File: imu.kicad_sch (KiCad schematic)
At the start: 3 parts, among them U14 LSM6DSV16XTR

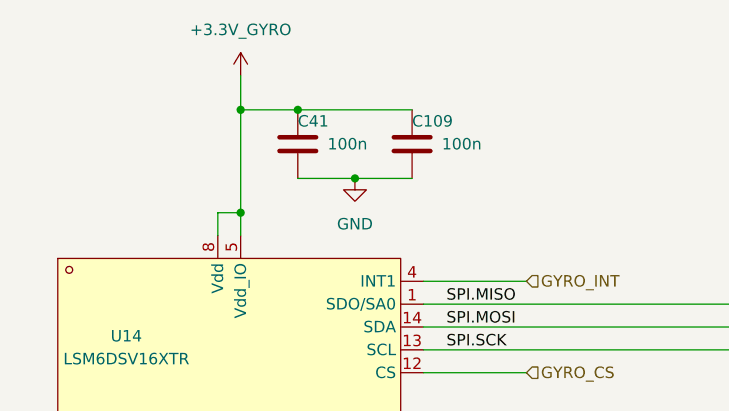
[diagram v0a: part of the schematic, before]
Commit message: fixed gyro power and rp2350 inductor
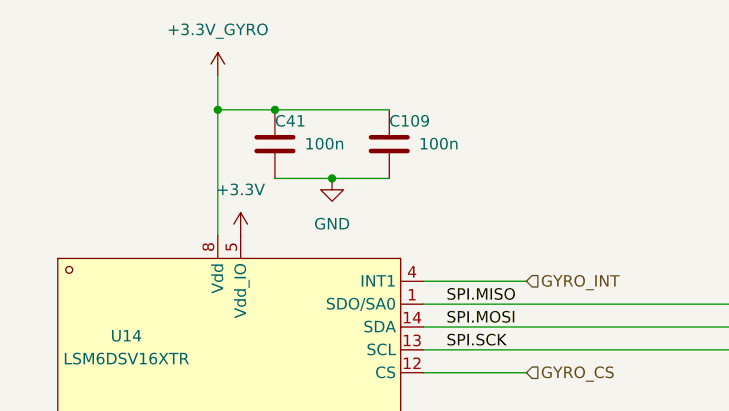
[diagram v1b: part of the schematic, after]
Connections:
- net +3.3V_GYRO: no longer U14.5 (Vdd_IO)
- new net +3.3V: U14.5 (Vdd_IO)
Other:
- moved on the sheet: C109, C41
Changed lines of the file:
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@@
 	(paper "A5")
 	(junction
-		(at 86.36 50.8)
+		(at 83.82 50.8)
 		(diameter 0)
 		(color 0 0 0 0)
@@
 	)
 	(junction
-		(at 73.66 43.18)
+		(at 71.12 43.18)
 		(diameter 0)
 		(color 0 0 0 0)
 	)
 	(junction
-		(at 80.01 43.18)
-		(diameter 0)
-		(color 0 0 0 0)
-	)
-	(junction
-		(at 73.66 54.61)
+		(at 77.47 43.18)
 		(diameter 0)
 		(color 0 0 0 0)
@@
 	(wire
 		(pts
-			(xy 73.66 43.18) (xy 80.01 43.18)
-		)
-		(stroke
-			(width 0)
-			(type default)
-		)
-	)
-	(wire
-		(pts
-			(xy 73.66 39.37) (xy 73.66 43.18)
-		)
-		(stroke
-			(width 0)
-			(type default)
-		)
-	)
-	(wire
-		(pts
-			(xy 80.01 43.18) (xy 92.71 43.18)
-		)
-		(stroke
-			(width 0)
-			(type default)
-		)
-	)
-	(wire
-		(pts
-			(xy 73.66 54.61) (xy 73.66 57.15)
-		)
-		(stroke
-			(width 0)
-			(type default)
-		)
-	)
-	(wire
-		(pts
-			(xy 71.12 57.15) (xy 71.12 54.61)
+			(xy 71.12 43.18) (xy 77.47 43.18)
+		)
+		(stroke
+			(width 0)
+			(type default)
+		)
+	)
+	(wire
+		(pts
+			(xy 71.12 39.37) (xy 71.12 43.18)
+		)
+		(stroke
+			(width 0)
+			(type default)
+		)
+	)
+	(wire
+		(pts
+			(xy 77.47 43.18) (xy 90.17 43.18)
 		)
 		(stroke
@@
 	(wire
 		(pts
-			(xy 86.36 50.8) (xy 92.71 50.8)
+			(xy 83.82 50.8) (xy 90.17 50.8)
 		)
 		(stroke
@@
 	(wire
 		(pts
-			(xy 71.12 54.61) (xy 73.66 54.61)
-		)
-		(stroke
-			(width 0)
-			(type default)
-		)
-	)
-	(wire
-		(pts
 			(xy 72.39 90.17) (xy 72.39 92.71)
 		)
@@
 	(wire
 		(pts
-			(xy 80.01 50.8) (xy 86.36 50.8)
-		)
-		(stroke
-			(width 0)
-			(type default)
-		)
-	)
-	(wire
-		(pts
-			(xy 73.66 43.18) (xy 73.66 54.61)
+			(xy 77.47 50.8) (xy 83.82 50.8)
+		)
+		(stroke
+			(width 0)
+			(type default)
+		)
+	)
+	(wire
+		(pts
+			(xy 71.12 43.18) (xy 71.12 57.15)
 		)
 		(stroke
@@
 	(symbol
 		(lib_id "power:+3.3V")
-		(at 73.66 39.37 0)
+		(at 71.12 39.37 0)
 		(unit 1)
 		(exclude_from_sim no)
@@
 		(fields_autoplaced yes)
 		(property "Reference" "#PWR0144"
-			(at 73.66 43.18 0)
+			(at 71.12 43.18 0)
 			(effects
 				(font
@@
 		)
 		(property "Value" "+3.3V_GYRO"
-			(at 73.66 34.29 0)
+			(at 71.12 34.29 0)
 			(effects
 				(font
@@
 		)
 		(property "Footprint" ""
-			(at 73.66 39.37 0)
+			(at 71.12 39.37 0)
 			(effects
 				(font
@@
 		)
 		(property "Datasheet" ""
-			(at 73.66 39.37 0)
+			(at 71.12 39.37 0)
 			(effects
 				(font
@@
 		)
 		(property "Description" "Power symbol creates a global label with name \"+3.3V\""
-			(at 73.66 39.37 0)
+			(at 71.12 39.37 0)
 			(effects
 				(font
@@
 	(symbol
 		(lib_id "Device:C")
-		(at 80.01 46.99 0)
+		(at 77.47 46.99 0)
 		(unit 1)
 		(exclude_from_sim no)
@@
 		(dnp no)
 		(property "Reference" "C41"
-			(at 80.01 44.45 0)
+			(at 77.47 44.45 0)
 			(effects
 				(font
@@
 		)
 		(property "Value" "100n"
-			(at 83.312 46.99 0)
+			(at 80.772 46.99 0)
 			(effects
 				(font
@@
 		)
 		(property "Footprint" "Capacitor_SMD:C_0402_1005Metric"
-			(at 80.9752 50.8 0)
+			(at 78.4352 50.8 0)
 			(effects
 				(font
@@
 		)
 		(property "Datasheet" "~"
-			(at 80.01 46.99 0)
+			(at 77.47 46.99 0)
 			(effects
 				(font
@@
 		)
 		(property "Description" ""
-			(at 80.01 46.99 0)
+			(at 77.47 46.99 0)
 			(effects
 				(font
@@
 		)
 		(property "LCSC" "C1525"
-			(at 80.01 46.99 0)
+			(at 77.47 46.99 0)
 			(effects
 				(font
@@
 	(symbol
 		(lib_id "Device:C")
-		(at 92.71 46.99 0)
+		(at 90.17 46.99 0)
 		(unit 1)
 		(exclude_from_sim no)
@@
 		(dnp no)
 		(property "Reference" "C109"
-			(at 92.71 44.45 0)
+			(at 90.17 44.45 0)
 			(effects
 				(font
@@
 		)
 		(property "Value" "100n"
-			(at 96.012 46.99 0)
+			(at 93.472 46.99 0)
 			(effects
 				(font
@@
 		)
 		(property "Footprint" "Capacitor_SMD:C_0402_1005Metric"
-			(at 93.6752 50.8 0)
+			(at 91.1352 50.8 0)
 			(effects
 				(font
@@
 		)
 		(property "Datasheet" "~"
-			(at 92.71 46.99 0)
+			(at 90.17 46.99 0)
 			(effects
 				(font
@@
 		)
 		(property "Description" ""
-			(at 92.71 46.99 0)
+			(at 90.17 46.99 0)
 			(effects
 				(font
@@
 		)
 		(property "LCSC" "C1525"
-			(at 92.71 46.99 0)
+			(at 90.17 46.99 0)
 			(effects
 				(font
@@
 	(symbol
 		(lib_id "power:GND")
-		(at 86.36 50.8 0)
+		(at 83.82 50.8 0)
 		(unit 1)
 		(exclude_from_sim no)
@@
 		(fields_autoplaced yes)
 		(property "Reference" "#PWR0146"
-			(at 86.36 57.15 0)
+			(at 83.82 57.15 0)
 			(effects
 				(font
@@
 		)
 		(property "Value" "GND"
-			(at 86.36 55.88 0)
+			(at 83.82 55.88 0)
 			(effects
 				(font
@@
 		)
 		(property "Footprint" ""
-			(at 86.36 50.8 0)
+			(at 83.82 50.8 0)
 			(effects
 				(font
@@
 		)
 		(property "Datasheet" ""
-			(at 86.36 50.8 0)
+			(at 83.82 50.8 0)
 			(effects
 				(font
@@
 		)
 		(property "Description" "Power symbol creates a global label with name \"GND\" , ground"
-			(at 86.36 50.8 0)
+			(at 83.82 50.8 0)
 			(effects
 				(font
@@
 					(unit 1)
 				)
+			)
+		)
+	)
+	(symbol
+		(lib_name "+3.3V_1")
+		(lib_id "power:+3.3V")
+		(at 73.66 57.15 0)
+		(unit 1)
+		(exclude_from_sim no)
+		(in_bom yes)
+		(on_board yes)
+		(dnp no)
+		(fields_autoplaced yes)
+		(property "Reference" "#PWR078"
+			(at 73.66 60.96 0)
+			(effects
+				(font
+					(size 1.27 1.27)
+				)
+				(hide yes)
+			)
+		)
+		(property "Value" "+3.3V"
+			(at 73.66 52.07 0)
+			(effects
+				(font
+					(size 1.27 1.27)
+				)
+			)
+		)
+		(property "Footprint" ""
+			(at 73.66 57.15 0)
+			(effects
+				(font
+					(size 1.27 1.27)
+				)
+				(hide yes)
+			)
+		)
+		(property "Datasheet" ""
+			(at 73.66 57.15 0)
+			(effects
+				(font
+					(size 1.27 1.27)
+				)
+				(hide yes)
+			)
+		)
+		(property "Description" "Power symbol creates a global label with name \"+3.3V\""
+			(at 73.66 57.15 0)
+			(effects
+				(font
+					(size 1.27 1.27)
+				)
+				(hide yes)
+			)
+		)
+		(pin "1"
+		)
+		(instances
+			(project "OpenFC"
+				(path "/fb88b6f9-ee39-4640-a9d4-04a17ceeac64/757ed1e6-9a5f-4a0e-a946-254eae8dfb0d"
+					(reference "#PWR078")
+					(unit 1)
+				)

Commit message: Switched to RP2354A and re-routed
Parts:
- removed C109: 100n, Capacitor_SMD:C_0402_1005Metric, symbol Device:C
- added C34: 100n, Capacitor_SMD:C_0402_1005Metric, symbol Device:C
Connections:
- net +3.3V: now also C34.1
- net GND: now also U14.2 (SDx/AH1/Qvar1), U14.3 (SCx/AH2/Qvar2), C34.2
- no-connect marks 5 -> 3

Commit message: Ordered first revision
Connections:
- net +3.3V_GYRO renamed +1.8V_GYRO

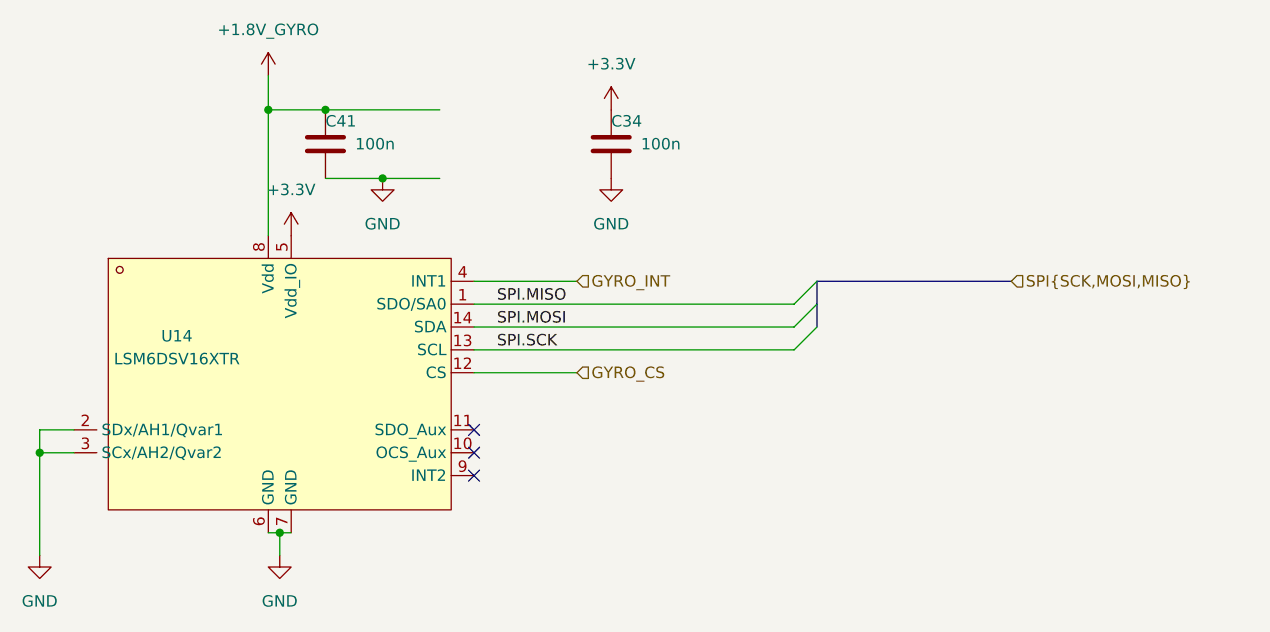
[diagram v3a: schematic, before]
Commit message: Switched to RP2354B for V2 of the FC for more IO. I want to try implement OSD on PIO state machine. I know BF already uses all of them but it should be possible and then later try to combine it witht the WS2812 protocol PIO2. If anybody here has any experience with analog OSD generation let me know, I just want to make a circuit that would allow further software development later. The reason I want to do it this way is it's cheap BOM<1 euro and low footprint, just 2 2x2 IC's and some passives.
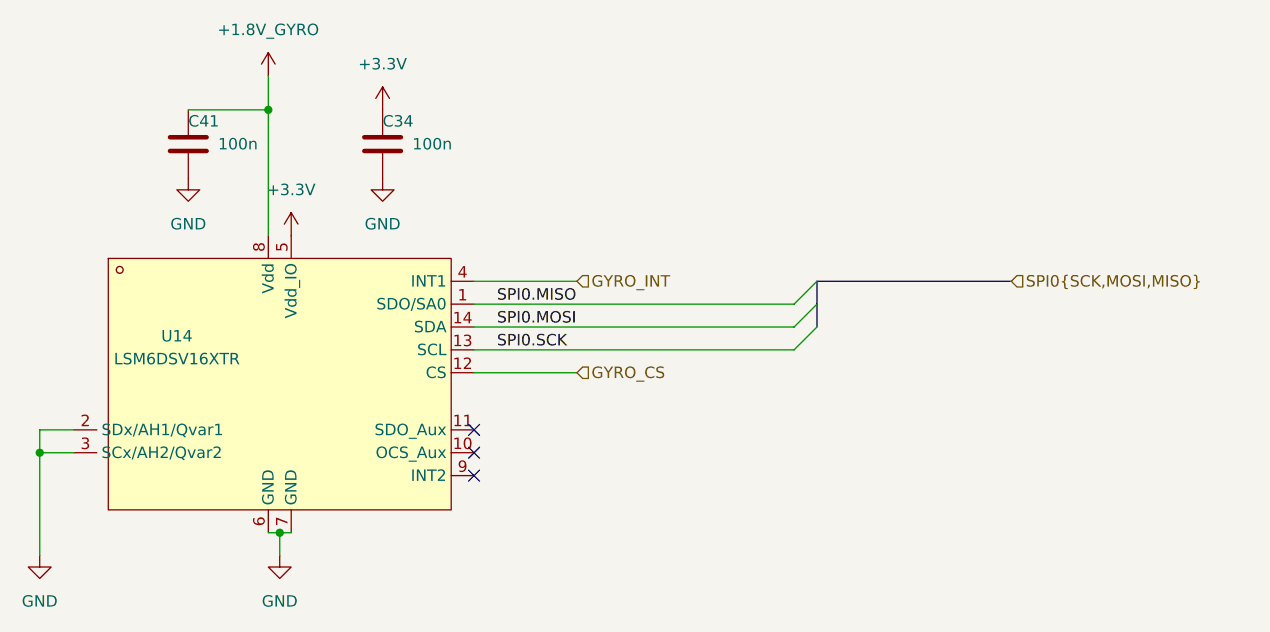
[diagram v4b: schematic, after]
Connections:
- net SPI.MISO renamed SPI0.MISO
- net SPI.MOSI renamed SPI0.MOSI
- net SPI.SCK renamed SPI0.SCK
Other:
- moved on the sheet: C34, C41
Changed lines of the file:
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@@
 	(paper "A5")
-	(junction
-		(at 83.82 50.8)
-		(diameter 0)
-		(color 0 0 0 0)
-	)
 	(junction
 		(at 72.39 90.17)
@@
 	)
 	(junction
-		(at 77.47 43.18)
-		(diameter 0)
-		(color 0 0 0 0)
-	)
-	(junction
 		(at 45.72 81.28)
 		(diameter 0)
@@
 	(wire
 		(pts
-			(xy 71.12 43.18) (xy 77.47 43.18)
-		)
-		(stroke
-			(width 0)
-			(type default)
-		)
-	)
-	(wire
-		(pts
 			(xy 71.12 39.37) (xy 71.12 43.18)
 		)
@@
 	(wire
 		(pts
-			(xy 77.47 43.18) (xy 90.17 43.18)
-		)
-		(stroke
-			(width 0)
-			(type default)
-		)
-	)
-	(wire
-		(pts
 			(xy 45.72 92.71) (xy 45.72 81.28)
 		)
@@
 	(wire
 		(pts
-			(xy 83.82 50.8) (xy 90.17 50.8)
-		)
-		(stroke
-			(width 0)
-			(type default)
-		)
-	)
-	(wire
-		(pts
 			(xy 93.98 62.23) (xy 105.41 62.23)
 		)
@@
 	(wire
 		(pts
+			(xy 62.23 43.18) (xy 71.12 43.18)
+		)
+		(stroke
+			(width 0)
+			(type default)
+		)
+	)
+	(wire
+		(pts
 			(xy 93.98 67.31) (xy 129.54 67.31)
 		)
@@
 	(wire
 		(pts
-			(xy 77.47 50.8) (xy 83.82 50.8)
-		)
-		(stroke
-			(width 0)
-			(type default)
-		)
-	)
-	(wire
-		(pts
 			(xy 45.72 78.74) (xy 49.53 78.74)
 		)
@@
 		)
 	)
-	(label "SPI.MOSI"
+	(label "SPI0.MOSI"
 		(at 96.52 67.31 0)
 		(effects
@@
 		)
 	)
-	(label "SPI.MISO"
+	(label "SPI0.MISO"
 		(at 96.52 64.77 0)
 		(effects
@@
 		)
 	)
-	(label "SPI.SCK"
+	(label "SPI0.SCK"
 		(at 96.52 69.85 0)
 		(effects
@@
 		)
 	)
-	(hierarchical_label "SPI{SCK,MOSI,MISO}"
+	(hierarchical_label "SPI0{SCK,MOSI,MISO}"
 		(shape input)
 		(at 153.67 62.23 0)
@@
 	(symbol
 		(lib_id "Device:C")
-		(at 77.47 46.99 0)
+		(at 62.23 46.99 0)
 		(unit 1)
 		(exclude_from_sim no)
@@
 		(dnp no)
 		(property "Reference" "C41"
-			(at 77.47 44.45 0)
+			(at 62.23 44.45 0)
 			(effects
 				(font
@@
 		)
 		(property "Value" "100n"
-			(at 80.772 46.99 0)
+			(at 65.532 46.99 0)
 			(effects
 				(font
@@
 		)
 		(property "Footprint" "Capacitor_SMD:C_0402_1005Metric"
-			(at 78.4352 50.8 0)
+			(at 63.1952 50.8 0)
 			(effects
 				(font
@@
 		)
 		(property "Datasheet" "~"
-			(at 77.47 46.99 0)
+			(at 62.23 46.99 0)
 			(effects
 				(font
@@
 		)
 		(property "Description" ""
-			(at 77.47 46.99 0)
+			(at 62.23 46.99 0)
 			(effects
 				(font
@@
 		)
 		(property "LCSC" "C1525"
-			(at 77.47 46.99 0)
+			(at 62.23 46.99 0)
 			(effects
 				(font
@@
 		(lib_name "+3.3V_1")
 		(lib_id "power:+3.3V")
-		(at 109.22 43.18 0)
+		(at 83.82 43.18 0)
 		(unit 1)
 		(exclude_from_sim no)
@@
 		(fields_autoplaced yes)
 		(property "Reference" "#PWR05"
-			(at 109.22 46.99 0)
+			(at 83.82 46.99 0)
 			(effects
 				(font
@@
 		)
 		(property "Value" "+3.3V"
-			(at 109.22 38.1 0)
+			(at 83.82 38.1 0)
 			(effects
 				(font
@@
 		)
 		(property "Footprint" ""
-			(at 109.22 43.18 0)
+			(at 83.82 43.18 0)
 			(effects
 				(font
@@
 		)
 		(property "Datasheet" ""
-			(at 109.22 43.18 0)
+			(at 83.82 43.18 0)
 			(effects
 				(font
@@
 		)
 		(property "Description" "Power symbol creates a global label with name \"+3.3V\""
-			(at 109.22 43.18 0)
+			(at 83.82 43.18 0)
 			(effects
 				(font
@@
 	(symbol
 		(lib_id "Device:C")
-		(at 109.22 46.99 0)
+		(at 83.82 46.99 0)
 		(unit 1)
 		(exclude_from_sim no)
@@
 		(dnp no)
 		(property "Reference" "C34"
-			(at 109.22 44.45 0)
+			(at 83.82 44.45 0)
 			(effects
 				(font
@@
 		)
 		(property "Value" "100n"
-			(at 112.522 46.99 0)
+			(at 87.122 46.99 0)
 			(effects
 				(font
@@
 		)
 		(property "Footprint" "Capacitor_SMD:C_0402_1005Metric"
-			(at 110.1852 50.8 0)
+			(at 84.7852 50.8 0)
 			(effects
 				(font
@@
 		)
 		(property "Datasheet" "~"
-			(at 109.22 46.99 0)
+			(at 83.82 46.99 0)
 			(effects
 				(font
@@
 		)
 		(property "Description" ""
-			(at 109.22 46.99 0)
+			(at 83.82 46.99 0)
 			(effects
 				(font
@@
 		)
 		(property "LCSC" "C1525"
-			(at 109.22 46.99 0)
+			(at 83.82 46.99 0)
 			(effects
 				(font
@@
 	(symbol
 		(lib_id "power:GND")
-		(at 109.22 50.8 0)
+		(at 83.82 50.8 0)
 		(unit 1)
 		(exclude_from_sim no)
@@
 		(fields_autoplaced yes)
 		(property "Reference" "#PWR010"
-			(at 109.22 57.15 0)
+			(at 83.82 57.15 0)
 			(effects
 				(font
@@
 		)
 		(property "Value" "GND"
-			(at 109.22 55.88 0)
+			(at 83.82 55.88 0)
 			(effects
 				(font
@@
 		)
 		(property "Footprint" ""
-			(at 109.22 50.8 0)
+			(at 83.82 50.8 0)
 			(effects
 				(font
@@
 		)
 		(property "Datasheet" ""
-			(at 109.22 50.8 0)
+			(at 83.82 50.8 0)
 			(effects
 				(font
@@
 		)
 		(property "Description" "Power symbol creates a global label with name \"GND\" , ground"
-			(at 109.22 50.8 0)
+			(at 83.82 50.8 0)
 			(effects
 				(font
@@
 	(symbol
 		(lib_id "power:GND")
-		(at 83.82 50.8 0)
+		(at 62.23 50.8 0)
 		(unit 1)
 		(exclude_from_sim no)
@@
 		(fields_autoplaced yes)
 		(property "Reference" "#PWR0146"
-			(at 83.82 57.15 0)
+			(at 62.23 57.15 0)
 			(effects
 				(font
@@
 		)
 		(property "Value" "GND"
-			(at 83.82 55.88 0)
+			(at 62.23 55.88 0)
 			(effects
 				(font
@@
 		)
 		(property "Footprint" ""
-			(at 83.82 50.8 0)
+			(at 62.23 50.8 0)
 			(effects
 				(font
@@
 		)
 		(property "Datasheet" ""
-			(at 83.82 50.8 0)
+			(at 62.23 50.8 0)
 			(effects
 				(font
@@
 		)
 		(property "Description" "Power symbol creates a global label with name \"GND\" , ground"
-			(at 83.82 50.8 0)
-			(effects
-				(font
+			(at 62.23 50.8 0)
+			(effects
+				(font
